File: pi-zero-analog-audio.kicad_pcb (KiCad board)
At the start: 2 copper layers, 65 x 30 mm, 22 parts, among them J1 GPIO, J2 SJ1-3555NG-BE, U1 LP5907MFX-3.3, U2 74LVC2G34

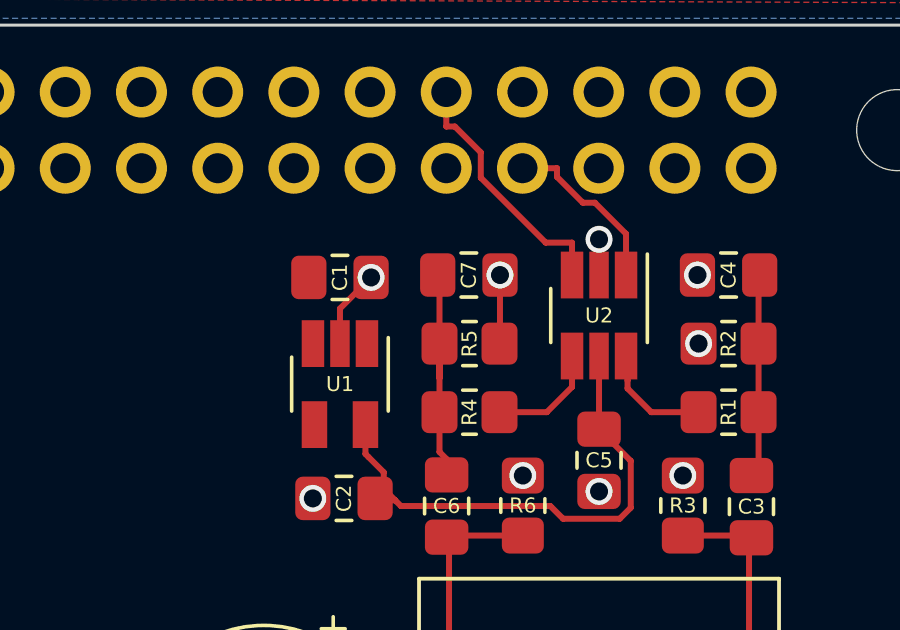
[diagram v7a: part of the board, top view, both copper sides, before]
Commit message: Adding gitignore + even more trying to make the footprint good for sc70 and sot-23
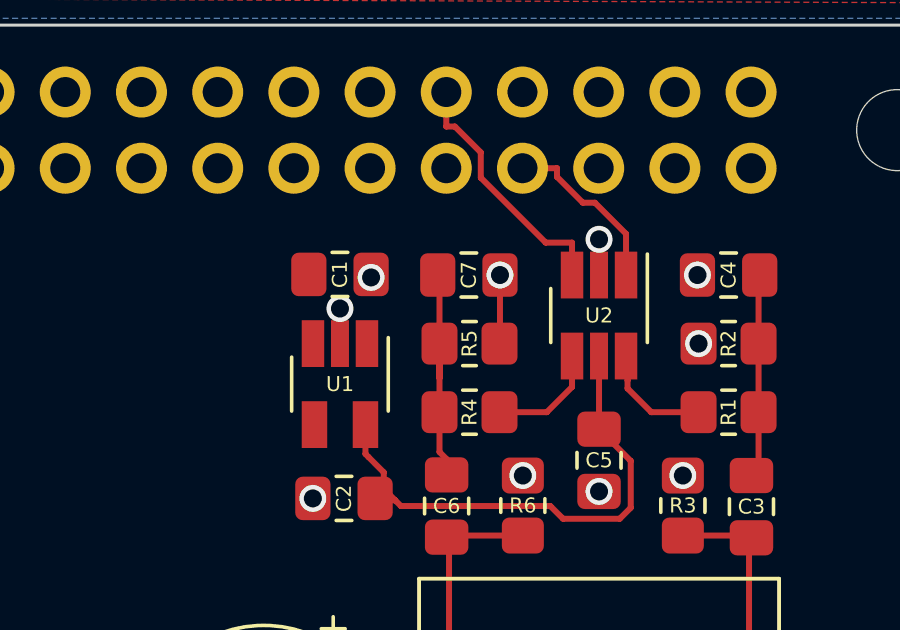
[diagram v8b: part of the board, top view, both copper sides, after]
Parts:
- moved C1 0.10 mm to (142.9, 78.3)
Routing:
- net GND: track 5.51 -> 2.87 mm, vias 9 -> 10
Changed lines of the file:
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@@
     (pad "1" smd rect (at -1.35 -0.9 270) (size 1.56 0.75) (layers "F.Cu" "F.Paste" "F.Mask")
       (net 25 "/PWM1") (pintype "input"))
-    (pad "2" smd rect (at -1.35 0 270) (size 1.56 0.65) (layers "F.Cu" "F.Paste" "F.Mask")
+    (pad "2" smd rect (at -1.35 0 270) (size 1.56 0.6) (layers "F.Cu" "F.Paste" "F.Mask")
       (net 1 "GND") (pinfunction "GND") (pintype "power_in"))
     (pad "3" smd rect (at -1.35 0.9 270) (size 1.56 0.75) (layers "F.Cu" "F.Paste" "F.Mask")
@@
     (pad "4" smd rect (at 1.35 0.9 270) (size 1.56 0.75) (layers "F.Cu" "F.Paste" "F.Mask")
       (net 38 "Net-(R4-Pad2)") (pintype "output"))
-    (pad "5" smd rect (at 1.35 0 270) (size 1.56 0.65) (layers "F.Cu" "F.Paste" "F.Mask")
+    (pad "5" smd rect (at 1.35 0 270) (size 1.56 0.6) (layers "F.Cu" "F.Paste" "F.Mask")
       (net 2 "VCC") (pinfunction "VCC") (pintype "power_in"))
     (pad "6" smd rect (at 1.35 -0.9 270) (size 1.56 0.75) (layers "F.Cu" "F.Paste" "F.Mask")
@@
   )
   (footprint "Capacitor_SMD:C_0805_2012Metric_Pad1.18x1.45mm_HandSolder" (layer "F.Cu")
-    (at 142.926 78.41)
+    (at 142.926 78.31)
     (descr "Capacitor SMD 0805 (2012 Metric), square (rectangular) end terminal, IPC_7351 nominal with elongated pad for handsoldering. (Body size source: IPC-SM-782 page 76, https://www.pcb-3d.com/wordpress/wp-content/uploads/ipc-sm-782a_amendment_1_and_2.pdf, https://docs.google.com/spreadsheets/d/1BsfQQcO9C6DZCsRaXUlFlo91Tg2WpOkGARC1WS5S8t0/edit?usp=sharing), generated with kicad-footprint-generator")
     (tags "capacitor handsolder")
@@
     (pad "1" smd rect (at -1.35 -0.9 270) (size 1.56 0.75) (layers "F.Cu" "F.Paste" "F.Mask")
       (net 29 "+5V") (pinfunction "IN") (pintype "power_in"))
-    (pad "2" smd rect (at -1.35 0 270) (size 1.56 0.65) (layers "F.Cu" "F.Paste" "F.Mask")
+    (pad "2" smd rect (at -1.35 0 270) (size 1.56 0.6) (layers "F.Cu" "F.Paste" "F.Mask")
       (net 1 "GND") (pinfunction "GND") (pintype "power_in"))
     (pad "3" smd rect (at -1.35 0.9 270) (size 1.56 0.75) (layers "F.Cu" "F.Paste" "F.Mask")
@@
   (gr_line (start 162 70) (end 103 70) (layer "Edge.Cuts") (width 0.1))
   (segment (start 151.562 77.14) (end 151.562 78.33) (width 0.2) (layer "F.Cu") (net 1))
-  (segment (start 142.926 79.4475) (end 142.926 80.616) (width 0.2) (layer "F.Cu") (net 1))
   (segment (start 148.26 78.33) (end 148.26 80.013) (width 0.2) (layer "F.Cu") (net 1))
-  (segment (start 143.9635 78.41) (end 142.926 79.4475) (width 0.2) (layer "F.Cu") (net 1))
   (via (at 149.022 85.014) (size 0.9) (drill 0.6) (layers "F.Cu" "B.Cu") (free) (net 1))
   (via (at 151.562 77.14) (size 0.9) (drill 0.6) (layers "F.Cu" "B.Cu") (net 1))
   (via (at 148.26 78.33) (size 0.9) (drill 0.6) (layers "F.Cu" "B.Cu") (net 1))
+  (via (at 142.926 79.4475) (size 0.9) (drill 0.6) (layers "F.Cu" "B.Cu") (net 1))
   (via (at 154.8425 78.33) (size 0.9) (drill 0.6) (layers "F.Cu" "B.Cu") (free) (net 1))
   (via (at 151.562 85.5435) (size 0.9) (drill 0.6) (layers "F.Cu" "B.Cu") (net 1))
